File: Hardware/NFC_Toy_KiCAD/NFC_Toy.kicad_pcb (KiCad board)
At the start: 2 copper layers, 113 parts, among them J1 Pad, J2 Pad, J3 JLink_Mini, J4 SPKR-, J5 SPKR+, J6 503182-1852, U1 TPS61032, U10 APA102, U11 APA102, U12 SN74LVC2T45, U13 APA102, U14 APA102, U15 APA102, U16 APA102, U17 APA102, U18 APA102, U19 MIC5225, U2 STM32L0-LQFP48, U3 LIS3DH, U4 MAX98357, U5 PN532, U6 APA102, U7 APA102, U8 APA102, U9 APA102, Y1 Oscillator

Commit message: Component placement complete.
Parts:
- added C49: 0.1u, Capacitors_SMD:C_0402, B.Cu at (62.0, 69.7)
- added C50: 0.1u, Capacitors_SMD:C_0402, B.Cu at (63.7, 59.8)
- added C51: 0.1u, Capacitors_SMD:C_0402, B.Cu at (70.2, 51.4)
- added C52: 0.1u, Capacitors_SMD:C_0402, B.Cu at (78.0, 45.5)
- added MK1: Mounting_Hole, Mounting_Holes:MountingHole_2.5mm, F.Cu at (59.1, 37.7)
- added MK2: Mounting_Hole, Mounting_Holes:MountingHole_2.5mm, F.Cu at (59.1, 93.0)
- added MK3: Mounting_Hole, Mounting_Holes:MountingHole_2.5mm, F.Cu at (178.9, 37.8)
- added MK4: Mounting_Hole, Mounting_Holes:MountingHole_2.5mm, F.Cu at (178.9, 92.8)
- added U20: APA102, NFC_Toy_Lib:APA102_hand_solder, B.Cu at (62.0, 65.4)
- added U21: APA102, NFC_Toy_Lib:APA102_hand_solder, B.Cu at (64.0, 55.4)
- added U22: APA102, NFC_Toy_Lib:APA102_hand_solder, B.Cu at (69.6, 46.9)
- added U23: APA102, NFC_Toy_Lib:APA102_hand_solder, B.Cu at (78.1, 41.3)
- C27, C35, C36, C37, C40, C41, C42, C43, C44, C45, C46, C47, C48, R11, R12, R13, R16, R17, R3, R4, R7, R8, R9, U10, U11, U13, U14, U15, U16, U17, U18, U6, U7, U8, U9: moved to B.Cu
- J3: footprint NFC_Toy_Lib:Socket_Strip_Straight_2x05_Pitch2.54mm_SMD_JLinkMini -> Socket_Strips:Socket_Strip_Straight_2x05_Pitch2.54mm_SMD
- R18, R19: value DNP -> 0; footprint Resistors_SMD:R_0603_HandSoldering -> Resistors_SMD:R_0402; moved to B.Cu
- moved TP15 218.3 mm to (266.4, 33.8)
- moved TP10 218.3 mm to (237.6, 29.1)
- moved TP12 218.3 mm to (261.3, 31.6)
- moved TP14 218.3 mm to (248.9, 36.4)
- moved TP3 218.3 mm to (250.0, 24.3)
- moved TP4 218.3 mm to (255.6, 25.4)
- moved TP5 218.3 mm to (241.3, 31.3)
- moved TP7 218.3 mm to (248.5, 30.1)
- moved TP1 218.3 mm to (239.3, 24.1)
- moved TP11 218.3 mm to (236.2, 35.6)
- moved TP13 218.3 mm to (244.2, 37.1)
- moved TP2 218.3 mm to (244.9, 24.3)
- moved TP6 218.3 mm to (244.9, 32.1)
- moved TP8 218.3 mm to (252.9, 32.1)
- moved TP9 218.3 mm to (256.9, 31.6)
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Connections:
- U18 pad 5: Net-(U18-Pad5) -> DotStar_CO_2
- U18 pad 6: Net-(U18-Pad6) -> DotStar_DO_2
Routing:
- net Net-(R17-Pad1): track 0.00 -> 377.8 mm, vias 0 -> 2
- net Net-(R16-Pad2): track 0.00 -> 377.7 mm, vias 0 -> 4
- net GND: track 0.00 -> 7.42 mm, vias 0 -> 1
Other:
- board outline added: 126 x 61.3 mm

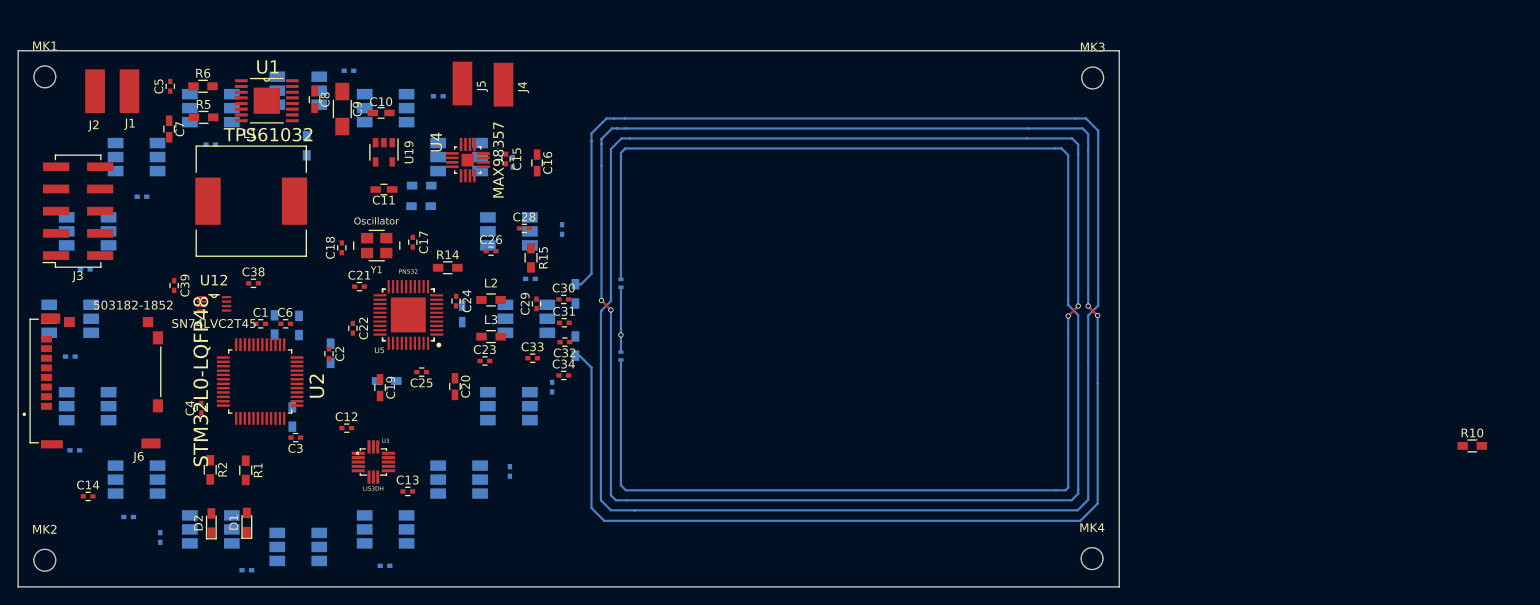
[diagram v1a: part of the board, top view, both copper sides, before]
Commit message: Layout 75% complete
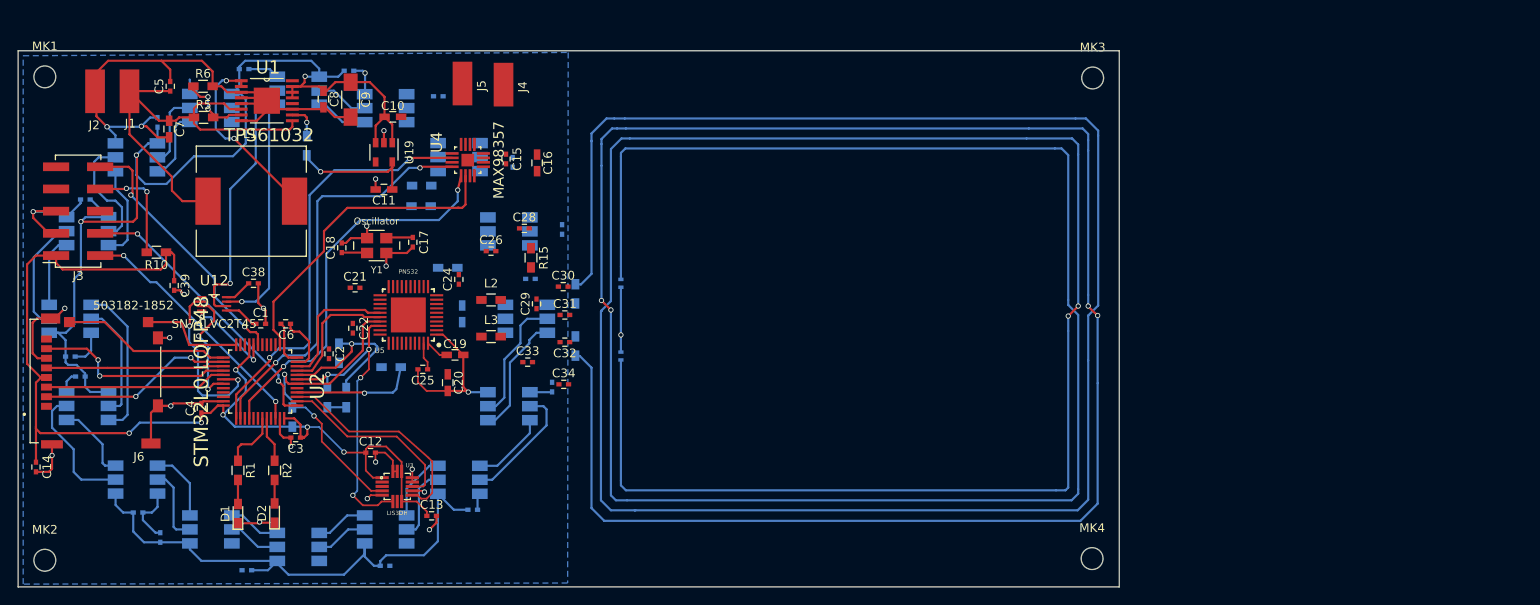
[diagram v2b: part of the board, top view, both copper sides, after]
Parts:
- removed C23: 0.1u, Capacitors_SMD:C_0402
- R14: moved to B.Cu
- moved R10 152.2 mm to (71.8, 57.8), turned to 180 degrees
- moved R9 10.3 mm to (91.4, 74.4), turned to 90 degrees
- moved R3 9.86 mm to (93.5, 74.4), turned to 90 degrees
- moved C52 9.44 mm to (81.9, 36.8)
- moved C19 9.36 mm to (106.0, 69.5), turned to 0 degrees
- moved C51 8.69 mm to (71.9, 42.9), turned to 90 degrees
- moved C48 8.47 mm to (63.1, 72.0), turned to 180 degrees
- moved C50 8.00 mm to (63.7, 51.8), turned to 180 degrees
- moved R2 7.37 mm to (85.3, 82.7)
- moved D2 7.33 mm to (85.3, 87.6)
- moved C14 6.85 mm to (58.0, 82.4), turned to 270 degrees
- moved C44 6.11 mm to (108.0, 87.2), turned to 0 degrees
- moved C13 3.91 mm to (103.3, 87.9)
- moved C12 3.91 mm to (96.3, 80.7)
- moved U3 3.91 mm to (99.4, 84.6)
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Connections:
- U2 pad 12: Net-(U2-Pad12) -> SD_DETECT
- U2 pad 13: Net-(U2-Pad13) -> SD_SW
- U2 pad 2: Net-(U2-Pad2) -> AUDIO_SD_N
- U2 pad 21: NFC_RST_PDN_N -> Net-(U2-Pad21)
- U2 pad 22: AUDIO_SD_N -> Net-(U2-Pad22)
- U2 pad 29: SD_DETECT -> Net-(U2-Pad29)
- U2 pad 30: SD_SW -> Net-(U2-Pad30)
- U2 pad 38: Net-(U2-Pad38) -> XL_INT1
- U2 pad 39: Net-(U2-Pad39) -> XL_INT2
- U2 pad 40: XL_INT2 -> NFC_RST_PDN_N
- U2 pad 41: XL_INT1 -> Net-(U2-Pad41)
- U2 pad 45: NFC_IRQ -> NFC_RST_N
- U2 pad 46: NFC_RST_N -> NFC_IRQ
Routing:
- net GND: track 7.42 -> 215.1 mm, vias 1 -> 25
- net +5V: track 0.00 -> 186.5 mm, vias 0 -> 3
- net +3V3: track 0.00 -> 153.4 mm, vias 0 -> 7
- net +BATT: track 0.00 -> 51.6 mm
- net I2S_WS: track 0.00 -> 48.8 mm, vias 0 -> 2
- net I2S_CK: track 0.00 -> 47.0 mm, vias 0 -> 2
- net I2S_SD: track 0.00 -> 44.5 mm, vias 0 -> 2
- net I2C_SDA: track 0.00 -> 37.8 mm, vias 0 -> 4
- net AUDIO_SD_N: track 0.00 -> 36.6 mm
- net I2C_SCL: track 0.00 -> 35.9 mm, vias 0 -> 2
- net SWCLK: track 0.00 -> 32.3 mm, vias 0 -> 2
- net DotStar_Clk_5V: track 0.00 -> 30.5 mm, vias 0 -> 1
- net nRST: track 0.00 -> 30.3 mm, vias 0 -> 2
- net SWDIO: track 0.00 -> 28.9 mm, vias 0 -> 2
- net DotStar_Data_5V: track 0.00 -> 27.3 mm, vias 0 -> 1
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- added copper zone on B.Cu, net GND
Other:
- net class skinny added: clearance 0.2, trace_width 0.2, via_dia 0.6, via_drill 0.4

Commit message: First pass layout complete
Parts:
- removed TP11: TEST, NFC_Toy_Lib:Test_Point
- moved TP4 189.4 mm to (69.8, 62.3), turned to 90 degrees
- moved SPI_CK 182.9 mm to (75.6, 79.2), turned to 90 degrees
- moved I2S_D 181.6 mm to (81.7, 79.0), turned to 90 degrees
- moved GND 181.1 mm to (71.4, 93.9)
- moved I2S_CK 180.4 mm to (79.5, 81.7), turned to 90 degrees
- moved SPI_MI 176.7 mm to (77.0, 79.2), turned to 90 degrees
- moved SPI_MO 174.1 mm to (74.2, 79.2), turned to 90 degrees
- moved DOT_CK 172.3 mm to (94.5, 45.4), turned to 90 degrees
- moved I2S_WS 172.0 mm to (79.5, 79.0), turned to 90 degrees
- moved I2C_D 165.6 mm to (91.8, 83.7), turned to 90 degrees
- moved I2C_Ck 158.0 mm to (89.3, 83.7), turned to 90 degrees
- moved DOT_D 157.0 mm to (92.2, 45.4), turned to 90 degrees
- moved ANT- 148.2 mm to (119.8, 75.7), turned to 90 degrees
- moved ANT+ 125.7 mm to (120.0, 57.2), turned to 90 degrees
- turned C21 to 180 degrees
- renumbered TP13 to ANT+, TP12 to ANT-, TP15 to DOT_CK, TP14 to DOT_D, TP5 to GND, TP10 to I2C_Ck, TP7 to I2C_D, TP8 to I2S_CK, TP9 to I2S_D, TP6 to I2S_WS, TP3 to SPI_CK, TP2 to SPI_MI, TP1 to SPI_MO
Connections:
- SPI_MO pad 1: SPI_MISO -> SPI_MOSI
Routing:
- net GND: track 215.1 -> 374.6 mm, vias 25 -> 56
- net +5V: track 186.5 -> 315.2 mm, vias 3 -> 12
- net +3V3: track 153.4 -> 242.2 mm, vias 7 -> 14
- net Net-(C29-Pad1): track 0.00 -> 26.8 mm, vias 0 -> 3
- net SPI_SCK: track 19.8 -> 41.3 mm, vias 0 -> 2
- net Net-(C28-Pad1): track 0.00 -> 16.2 mm, vias 0 -> 2
- net VCC: track 3.17 -> 18.4 mm, vias 0 -> 3
- net DotStar_CO_0: track 0.00 -> 14.4 mm
- net DotStar_DO_0: track 0.00 -> 13.4 mm
- net (no net): track 0.00 -> 13.1 mm, vias 0 -> 6
- net Net-(R11-Pad2): track 0.00 -> 12.4 mm, vias 0 -> 1
- net SPI_NSS: track 22.3 -> 34.7 mm, vias 2 -> 3
- net Net-(U13-Pad5): track 0.00 -> 12.0 mm
- net Net-(C31-Pad2): track 0.00 -> 11.6 mm
- net Net-(U13-Pad6): track 0.00 -> 11.5 mm
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- added copper zone on F.Cu, net GND

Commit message: Preliminary layout complete
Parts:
- added GND1: TEST, NFC_Toy_Lib:Test_Point, F.Cu at (60.3, 42.3)
- added GND2: TEST, NFC_Toy_Lib:Test_Point, F.Cu at (116.6, 41.2)
- added GND3: TEST, NFC_Toy_Lib:Test_Point, F.Cu at (112.0, 93.0)
- added GND4: TEST, NFC_Toy_Lib:Test_Point, F.Cu at (122.7, 89.4)
- added GND4: TEST, NFC_Toy_Lib:Test_Point, F.Cu at (123.0, 41.6)
- moved SPI_MI 0.05 mm to (77.0, 79.2), turned to 270 degrees
- renumbered GND to GND0, TP4 to SPI_NSS
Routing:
- net GND: track 374.6 -> 443.1 mm, vias 56 -> 64
- net (no net): track 13.1 -> 9.77 mm, vias 6 -> 4
- net VCC: track 18.4 -> 20.4 mm
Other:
- net class Default: clearance 0.2 -> 0.15
- net class skinny: clearance 0.2 -> 0.15
- rule pad_to_mask_clearance: 0.2 -> 0.0508
- rule trace_clearance: 0.2 -> 0.15
- board text added: "AC"
- board text added: "NFC Fun"

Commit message: Submitted to PCBWay for build
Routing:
- net GND: track 443.1 -> 456.0 mm, vias 64 -> 68
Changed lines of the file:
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@@
   (general
     (links 318)
-    (no_connects 1)
+    (no_connects 0)
     (area 53.500238 33.294 184.497763 97.5525)
     (thickness 1.6)
     (drawings 9)
-    (tracks 1524)
+    (tracks 1541)
     (zones 0)
     (modules 128)
@@
     (mod_text_size 1 1)
     (mod_text_width 0.15)
-    (pad_size 0.75 1)
+    (pad_size 0.3048 1.45)
     (pad_drill 0)
     (pad_to_mask_clearance 0.0508)
@@
     (visible_elements 7FFEFF7F)
     (pcbplotparams
-      (layerselection 0x0103c_80000001)
+      (layerselection 0x010fc_80000001)
       (usegerberextensions false)
       (excludeedgelayer true)
@@
     (pad 4 smd rect (at -1.7914 0.762) (size 0.3048 1.5) (layers F.Cu F.Paste F.Mask)
       (net 45 "Net-(R11-Pad2)"))
-    (pad 5 smd rect (at -0.762 1.7914 270) (size 0.3048 1.5) (layers F.Cu F.Paste F.Mask)
+    (pad 5 smd rect (at -0.762 1.8414 270) (size 0.3048 1.45) (layers F.Cu F.Paste F.Mask)
       (net 75 "Net-(U4-Pad5)"))
     (pad 6 smd rect (at -0.254 1.7914 270) (size 0.3048 1.5) (layers F.Cu F.Paste F.Mask)
@@
     (pad 7 smd rect (at 0.254 1.7914 270) (size 0.3048 1.5) (layers F.Cu F.Paste F.Mask)
       (net 4 +5V))
-    (pad 8 smd rect (at 0.762 1.7914 270) (size 0.3048 1.5) (layers F.Cu F.Paste F.Mask)
+    (pad 8 smd rect (at 0.762 1.8414 270) (size 0.3048 1.45) (layers F.Cu F.Paste F.Mask)
       (net 4 +5V))
     (pad 9 smd rect (at 1.7914 0.762) (size 0.3048 1.5) (layers F.Cu F.Paste F.Mask)
@@
     (pad 12 smd rect (at 1.7914 -0.762) (size 0.3048 1.5) (layers F.Cu F.Paste F.Mask)
       (net 77 "Net-(U4-Pad12)"))
-    (pad 13 smd rect (at 0.762 -1.7914 270) (size 0.3048 1.5) (layers F.Cu F.Paste F.Mask)
+    (pad 13 smd rect (at 0.762 -1.8414 270) (size 0.3048 1.45) (layers F.Cu F.Paste F.Mask)
       (net 78 "Net-(U4-Pad13)"))
     (pad 14 smd rect (at 0.254 -1.7914 270) (size 0.3048 1.5) (layers F.Cu F.Paste F.Mask)
@@
     (pad 15 smd rect (at -0.254 -1.7914 270) (size 0.3048 1.5) (layers F.Cu F.Paste F.Mask)
       (net 2 GND))
-    (pad 16 smd rect (at -0.762 -1.7914 270) (size 0.3048 1.5) (layers F.Cu F.Paste F.Mask)
+    (pad 16 smd rect (at -0.762 -1.8414 270) (size 0.3048 1.45) (layers F.Cu F.Paste F.Mask)
       (net 50 I2S_CK))
     (pad 17 smd rect (at 0 0 90) (size 1.4478 1.4478) (layers F.Cu F.Paste F.Mask)
@@
     (pad 31 smd rect (at 2.25 -3.24 180) (size 0.25 1.5) (layers F.Cu F.Paste F.Mask)
       (net 80 "Net-(U5-Pad31)"))
-    (pad 30 smd rect (at 3.24 -2.25 90) (size 0.25 1.5) (layers F.Cu F.Paste F.Mask)
+    (pad 30 smd rect (at 3.29 -2.25 90) (size 0.25 1.45) (layers F.Cu F.Paste F.Mask)
       (net 81 "Net-(U5-Pad30)"))
     (pad 29 smd rect (at 3.24 -1.75 90) (size 0.25 1.5) (layers F.Cu F.Paste F.Mask)
@@
     (pad 22 smd rect (at 3.24 1.75 90) (size 0.25 1.5) (layers F.Cu F.Paste F.Mask)
       (net 84 "Net-(U5-Pad22)"))
-    (pad 21 smd rect (at 3.24 2.25 90) (size 0.25 1.5) (layers F.Cu F.Paste F.Mask)
+    (pad 21 smd rect (at 3.29 2.25 90) (size 0.25 1.45) (layers F.Cu F.Paste F.Mask)
       (net 85 "Net-(U5-Pad21)"))
     (pad 20 smd rect (at 2.25 3.24) (size 0.25 1.5) (layers F.Cu F.Paste F.Mask)
@@
     (pad 11 smd rect (at -2.25 3.24) (size 0.25 1.5) (layers F.Cu F.Paste F.Mask)
       (net 2 GND))
-    (pad 10 smd rect (at -3.24 2.25 270) (size 0.25 1.5) (layers F.Cu F.Paste F.Mask)
+    (pad 10 smd rect (at -3.29 2.25 270) (size 0.25 1.45) (layers F.Cu F.Paste F.Mask)
       (net 10 "Net-(C28-Pad1)"))
     (pad 9 smd rect (at -3.24 1.75 270) (size 0.25 1.5) (layers F.Cu F.Paste F.Mask)
@@
     (pad 39 smd rect (at -1.75 -3.24 180) (size 0.25 1.5) (layers F.Cu F.Paste F.Mask)
       (net 8 VCC))
-    (pad 40 smd rect (at -2.25 -3.24 180) (size 0.25 1.5) (layers F.Cu F.Paste F.Mask)
+    (pad 40 smd rect (at -2.25 -3.29 180) (size 0.25 1.45) (layers F.Cu F.Paste F.Mask)
       (net 1 +3V3))
   )
@@
   (segment (start 89.027 46.99) (end 89.027 46.693) (width 0.25) (layer B.Cu) (net 1))
   (segment (start 98.8035 47.455) (end 98.8035 50.6095) (width 0.25) (layer F.Cu) (net 1))
+  (segment (start 77.0255 65.2145) (end 76.8477 65.2145) (width 0.25) (layer B.Cu) (net 2))
+  (via (at 74.9935 62.611) (size 0.6) (drill 0.4) (layers F.Cu B.Cu) (net 2))
+  (segment (start 74.9935 63.3603) (end 74.9935 62.611) (width 0.25) (layer B.Cu) (net 2))
+  (segment (start 76.8477 65.2145) (end 74.9935 63.3603) (width 0.25) (layer B.Cu) (net 2))
+  (segment (start 64.8015 39.37) (end 66.802 39.37) (width 0.25) (layer F.Cu) (net 2))
+  (segment (start 66.7512 39.3192) (end 66.7512 39.2684) (width 0.25) (layer B.Cu) (net 2))
+  (segment (start 66.802 39.37) (end 66.7512 39.3192) (width 0.25) (layer B.Cu) (net 2))
+  (via (at 66.802 39.37) (size 0.6) (drill 0.4) (layers F.Cu B.Cu) (net 2))
+  (segment (start 64.8015 39.37) (end 64.8015 39.6941) (width 0.25) (layer F.Cu) (net 2))
+  (segment (start 64.8015 39.6941) (end 63.7032 40.7924) (width 0.25) (layer F.Cu) (net 2))
+  (segment (start 63.7032 40.7924) (end 62.8904 40.7924) (width 0.25) (layer F.Cu) (net 2))
+  (via (at 62.8904 40.7924) (size 0.6) (drill 0.4) (layers F.Cu B.Cu) (net 2))
+  (segment (start 64.8015 39.37) (end 64.8015 39.1475) (width 0.25) (layer F.Cu) (net 2))
+  (segment (start 64.8015 39.1475) (end 63.5508 37.8968) (width 0.25) (layer F.Cu) (net 2))
+  (via (at 62.8396 37.8968) (size 0.6) (drill 0.4) (layers F.Cu B.Cu) (net 2))
+  (segment (start 63.5508 37.8968) (end 62.8396 37.8968) (width 0.25) (layer F.Cu) (net 2))
+  (segment (start 64.8015 39.37) (end 62.9412 39.37) (width 0.25) (layer F.Cu) (net 2))
+  (via (at 62.9412 39.37) (size 0.6) (drill 0.4) (layers F.Cu B.Cu) (net 2))
   (segment (start 82.9056 70.5612) (end 83.1596 70.5612) (width 0.25) (layer F.Cu) (net 2))
   (segment (start 84.582 69.1388) (end 84.582 66.9544) (width 0.25) (layer B.Cu) (net 2))
@@
   (segment (start 84.4296 65.9384) (end 84.4296 66.802) (width 0.25) (layer B.Cu) (net 2))
   (segment (start 74.9935 62.611) (end 74.9935 62.6745) (width 0.25) (layer F.Cu) (net 2))
+  (segment (start 74.9935 62.6745) (end 73.1012 64.5668) (width 0.25) (layer F.Cu) (net 2))
+  (via (at 73.1012 64.5668) (size 0.6) (drill 0.4) (layers F.Cu B.Cu) (net 2))
   (segment (start 74.5275 62.145) (end 74.9935 62.611) (width 0.25) (layer F.Cu) (net 2))
-  (via (at 74.9935 62.611) (size 0.6) (drill 0.4) (layers F.Cu B.Cu) (net 2))
   (segment (start 73.8505 62.145) (end 74.5275 62.145) (width 0.25) (layer F.Cu) (net 2))
-  (via (at 73.1012 64.5668) (size 0.6) (drill 0.4) (layers F.Cu B.Cu) (net 2))
-  (segment (start 74.9935 62.6745) (end 73.1012 64.5668) (width 0.25) (layer F.Cu) (net 2))
   (segment (start 71.9955 75.357) (end 70.312 75.357) (width 0.25) (layer F.Cu) (net 2))
   (via (at 70.2945 75.3745) (size 0.6) (drill 0.4) (layers F.Cu B.Cu) (net 2))
